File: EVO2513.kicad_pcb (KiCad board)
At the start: 8 copper layers, 110 x 69 mm, 260 parts, among them J1 1053101204, J2 1053101114, J3 10144517-043802LF, J4 1053102204, J5 1053091102, J6 1053091102, M1 78614150960, M2 78614150960, M3 78614150960, M4 78614150960, M5 78614150960, M6 78614150960, Q1 DMT6007LFGQ-7, Q10 DMT4011LFG, Q11 DMT4011LFG, Q12 DMP3007SCG-13, Q13 DMP3007SCG-13, Q14 DMP3007SCG-13, Q15 DMP3007SCG-13, Q16 IAUCN04S7L019, Q17 IAUCN04S7L028, Q18 CSD17304Q3, Q19 IAUCN04S7L019, Q20 BSS138, Q21 BSS138, Q22 BSS138, Q23 BSS138, Q24 BSS138, Q3 DMT6007LFGQ-7, Q4 DMP3007SCG-13, Q5 DMP3007SCG-13, Q6 DMT4011LFG, Q7 DMT4011LFG, Q8 DMT4011LFG, Q9 DMT4011LFG, U1 LTC1960, U10 TLV9002IDSG, U11 PCAL9714, U2 LTC4365, U5 LM51772RHAR, U6 TPS22811, U7 TPS22811, U8 TLV9002IDSG, U9 TPS22811

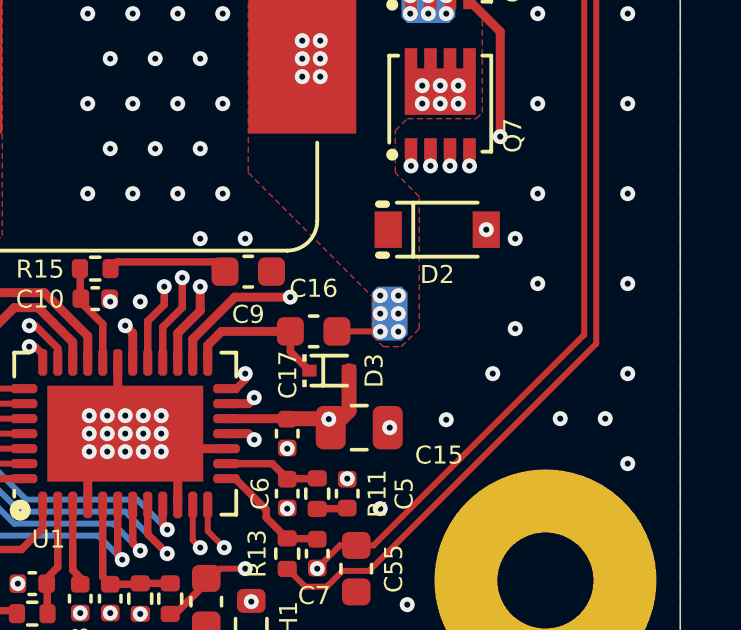
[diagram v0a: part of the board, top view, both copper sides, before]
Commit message: Add D5: DNP alternate for D2 at its original 0.5.0 position
- S04: D5 (SS0540, SOD-123) in parallel with D2 on the charger switch
  node and GND, marked DNP, with a NOTE explaining it is an alternate
  to D2.
- PCB: D5 placed where D2 sat on the Altium 0.5.0 board (pads at
  195.70/126.27 and 195.70/129.54, rotated 270). The Net-(D2-C) F.Cu
  pour gets a small tab to reach the D5 cathode; the anode is in the
  GND pour. Zones refilled.
- The board diff is mostly KiCad re-sorting the FET paste-window pads
  on save; no other geometry changed.

ERC 0. DRC: 0 unconnected, 0 parity; remaining items unchanged
(excluded layer-marker edge clearances, silk overlap, text thickness).

Co-Authored-By: Claude Opus 5.5 <noreply@anthropic.com>
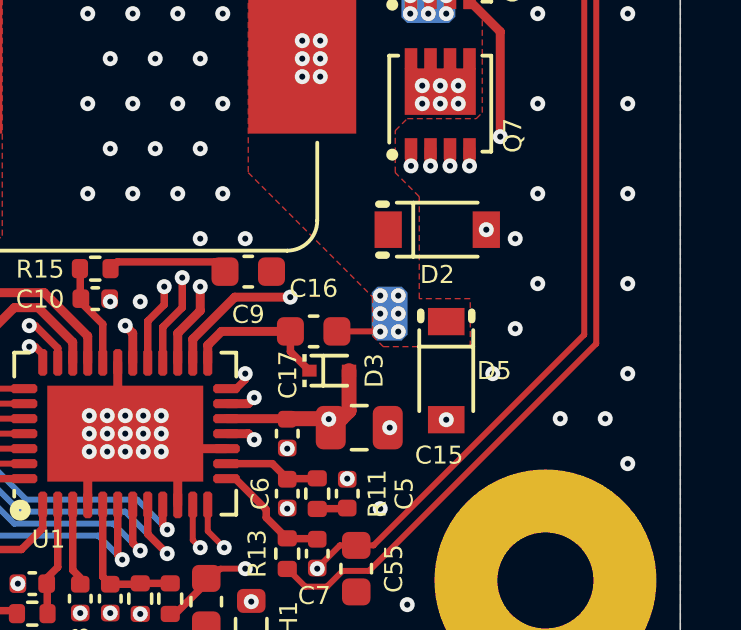
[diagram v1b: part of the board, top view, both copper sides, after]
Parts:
- added D5: SS0540 40V, EVO2513-0_5_0-import-fps:Diode SOD123, F.Cu at (195.7, 127.9)
